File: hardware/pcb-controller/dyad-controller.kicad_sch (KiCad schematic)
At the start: 40 parts, among them J1 USB_C_Receptacle_USB2.0, J10 USB-C split link, J2 SWD, J6 HC-FPC-0.5-20P-FH20, J7 HC-FPC-0.5-20P-FH20, J8 HC-FPC-0.5-14P-FH20, J9 USB-C split link, SW1 SW_Push, U1 W25Q128JVS, U2 USBLC6-2SC6, U3 RP2040, U4 XC6206PxxxMR-Regulator_Linear, Y1 12MHz

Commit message: Fit real BOOTSEL and RESET buttons
CONTROLLER.md §4 items 2 and 3, the two it flags as "would ship a broken or
unflashable board if missed".

SW1's BOOTSEL "switch" was a PinSocket_1x02 header inherited from the dev
board -- a pin header you short with tweezers, not a button. It now carries
Button_Switch_SMD:SW_Push_1P1T_XKB_TS-1187A. SW2 is new, from ~{RESET} to
GND; ~{RESET} is the RP2040's RUN (U3 pin 26), already pulled up by R2 and
brought out to the SWD header, so the button only has to pull it down.

Part: TS-1187A-B-A-B, C318884, JLCPCB **Basic** with 679k stock, 5.1 x 5.1 mm
SMD. One BOM line covers both buttons. KiCad ships a footprint for exactly
this family, and its pads are numbered 1,1,2,2 rather than 1,2,3,4, so the
2-pin SW_Push symbol maps onto the 4-pad part without a symbol change.
Chosen over the TS-1187A-S16 and K2-1114SA alternatives, which are Extended
with 3k-56k stock.

One self-inflicted warning, found and fixed rather than committed: wiring
SW2 raised same_local_global_label, because ~{RESET} exists as a *global*
label on this sheet while batch_connect_to_net only writes local ones.
Replaced with a global label; the warning cleared and the net reads back as
U3 pin 26 + R2 + J2 + SW2. Recorded in §5 step 3 as a trap for the next
signal wired to a global label.

Numbers: errors unchanged at 3, still only GPIO27-29, the genuine spares.
Every other count identical -- endpoint_off_grid 92, lib_symbol_mismatch 48.
0 shorts, 0 orphans.

That closes every unconditional item in §4 except the DNP level shifter. The
only other outstanding change is the LDO swap, which is gated on a Phase 1
current measurement.

Co-Authored-By: Claude Opus 5 <noreply@anthropic.com>
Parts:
- added SW2: RESET, Button_Switch_SMD:SW_Push_1P1T_XKB_TS-1187A, symbol Switch:SW_Push
- SW1: value SW_Push -> BOOTSEL; footprint Connector_PinSocket_2.54mm:PinSocket_1x02_P2.54mm_Vertical -> Button_Switch_SMD:SW_Push_1P1T_XKB_TS-1187A; LCSC (none) -> C318884
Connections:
- net GND: now also SW2.2
- net ~{RESET}: now also SW2.1
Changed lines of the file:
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@@
 		)
 	)
+	(label "VBUS_FUSED"
+		(at 272.415 29.21 0)
+		(effects
+			(font
+				(size 1.27 1.27)
+			)
+			(justify left bottom)
+		)
+	)
+	(label "VBUS_FUSED"
+		(at 144.78 175.26 0)
+		(effects
+			(font
+				(size 1.27 1.27)
+			)
+			(justify left bottom)
+		)
+	)
+	(label "+5V"
+		(at 137.16 175.26 180)
+		(effects
+			(font
+				(size 1.27 1.27)
+			)
+			(justify right bottom)
+		)
+	)
+	(label "+5V"
+		(at 140.97 199.39 0)
+		(effects
+			(font
+				(size 1.27 1.27)
+			)
+			(justify left bottom)
+		)
+	)
+	(label "VBUS_SPLIT"
+		(at 140.97 194.31 0)
+		(effects
+			(font
+				(size 1.27 1.27)
+			)
+			(justify left bottom)
+		)
+	)
+	(label "GND"
+		(at 146.05 218.44 0)
+		(effects
+			(font
+				(size 1.27 1.27)
+			)
+			(justify left bottom)
+		)
+	)
 	(global_label "SWCLK"
 		(shape input)
@@
 		)
 	)
-  (label "VBUS_FUSED"
-    (at 272.415 29.21 0)
-    (fields_autoplaced yes)
-    (effects (font (size 1.27 1.27)) (justify left bottom))
-  )
-  (label "VBUS_FUSED"
-    (at 144.78 175.26 0)
-    (fields_autoplaced yes)
-    (effects (font (size 1.27 1.27)) (justify left bottom))
-  )
-  (label "+5V"
-    (at 137.16 175.26 180)
-    (fields_autoplaced yes)
-    (effects (font (size 1.27 1.27)) (justify right bottom))
-  )
-  (label "+5V"
-    (at 140.97 199.39 0)
-    (fields_autoplaced yes)
-    (effects (font (size 1.27 1.27)) (justify left bottom))
-  )
-  (label "VBUS_SPLIT"
-    (at 140.97 194.31 0)
-    (fields_autoplaced yes)
-    (effects (font (size 1.27 1.27)) (justify left bottom))
-  )
+	(global_label "~{RESET}"
+		(shape input)
+		(at 135.89 218.44 180)
+		(effects
+			(font
+				(size 1.27 1.27)
+			)
+			(justify right)
+		)
+	)
 	(symbol
 		(lib_id "Device:R_Small")
@@
 			)
 		)
-		(property "Value" "SW_Push"
+		(property "Value" "BOOTSEL"
 			(at 118.11 21.59 0)
 			(show_name no)
@@
 			)
 		)
-		(property "Footprint" "Connector_PinSocket_2.54mm:PinSocket_1x02_P2.54mm_Vertical"
+		(property "Footprint" "Button_Switch_SMD:SW_Push_1P1T_XKB_TS-1187A"
 			(at 118.11 21.59 0)
 			(hide yes)
@@
 			)
 		)
+		(property "LCSC" "C318884"
+			(at 118.11 26.67 0)
+			(hide yes)
+			(effects
+				(font
+					(size 1.27 1.27)
+				)
+			)
+		)
 		(body_style 1)
 		(in_pos_files yes)
@@
 			)
 		)
-		(instances
-			(project "dyad-controller"
-				(path "/ba62e47e-9e07-4e97-ab08-24b670d50f97"
-					(reference "D1")
-					(unit 1)
-				)
-			)
-		)
 		(property "LCSC" "C8678"
 			(at 140.97 175.26 0)
@@
 				)
 			)
-		))
+		)
+		(instances
+			(project "dyad-controller"
+				(path "/ba62e47e-9e07-4e97-ab08-24b670d50f97"
+					(reference "D1")
+					(unit 1)
+				)
+			)
+		)
+	)
 	(symbol
 		(lib_id "Device:Polyfuse_Small")
@@
 			)
 		)
+		(property "LCSC" "C70076"
+			(at 140.97 196.85 0)
+			(hide yes)
+			(effects
+				(font
+					(size 1.27 1.27)
+				)
+			)
+		)
 		(instances
 			(project "dyad-controller"
@@
 			)
 		)
-		(property "LCSC" "C70076"
-			(at 140.97 196.85 0)
+	)
+	(symbol
+		(lib_id "Switch:SW_Push")
+		(at 140.97 218.44 0)
+		(unit 1)
+		(in_bom yes)
+		(on_board yes)
+		(dnp no)
+		(property "Reference" "SW2"
+			(at 142.24 215.9 0)
+			(effects
+				(font
+					(size 1.27 1.27)
+				)
+				(justify left)
+			)
+		)
+		(property "Value" "RESET"
+			(at 140.97 219.964 0)
+			(effects
+				(font
+					(size 1.27 1.27)
+				)
+			)
+		)
+		(property "Footprint" "Button_Switch_SMD:SW_Push_1P1T_XKB_TS-1187A"
+			(at 140.97 218.44 0)
+			(hide yes)
+			(effects
+				(font
+					(size 1.27 1.27)
+				)
+			)
+		)
+		(property "Datasheet" ""
+			(at 140.97 218.44 0)
+			(hide yes)
+			(effects
+				(font
+					(size 1.27 1.27)
+				)
+			)
+		)
+		(property "Description" "Push button switch, generic, two pins"
+			(at 140.97 218.44 0)
 			(hide yes)
 			(effects
@@
 				)
 			)
-		))
+		)
+		(property "LCSC" "C318884"
+			(at 140.97 218.44 0)
+			(hide yes)
+			(effects
+				(font
+					(size 1.27 1.27)
+				)
+			)
+		)
+		(instances
+			(project "dyad-controller"
+				(path "/ba62e47e-9e07-4e97-ab08-24b670d50f97"
+					(reference "SW2")
+					(unit 1)
+				)
+			)
+		)
+	)
 	(polyline
 		(pts

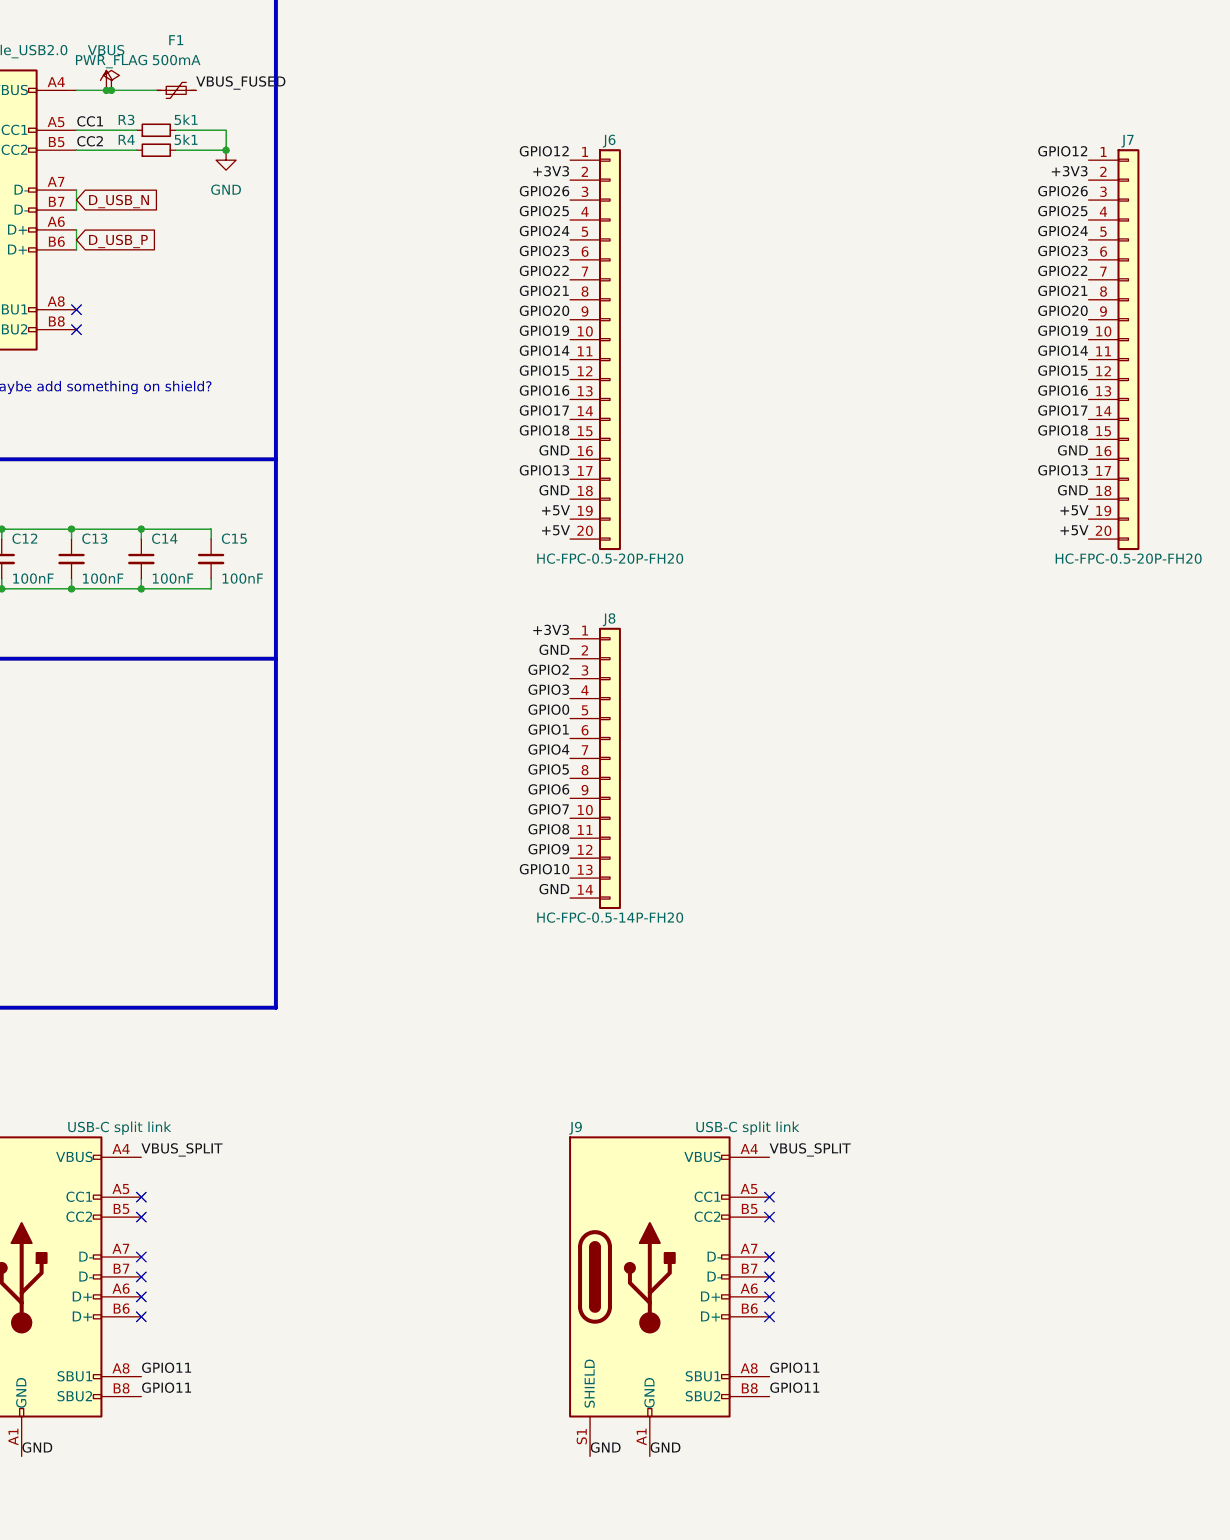
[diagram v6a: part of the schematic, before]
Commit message: Reassign the controller GPIOs to match the board's geometry
The first pin map predated any placement and put the knob bus on the side
of the RP2040 facing away from the knob FFC. With parts on B.Cu, a 35 x 50
board and U3's USB face toward the rear, the knob now takes GP16-26 off the
front-left corner, keeping the SPI0/I2C0 dual-function pair on GP16/GP17,
and the matrix, LEDIN and SPLIT take GP0-15 as one bundle already in J7's
pad order. GP27-29 stay spare and ADC-capable.

Applied by renaming only the connector-side net labels, so U3's labels
still name the physical pin. J8 pins 3-6 reorder to D0, D1, SCK, MOSI; the
knob module does not exist yet. Netlist verified pin by pin; ERC unchanged
at 152 findings with the same 3 errors.

CONTROLLER.md records the map, the connector pin-1 geometry it was derived
from, and the routing consequence: J6 is reached by wrapping the bundle
around the rear of the chip, which supplies the order reversal J6 needs,
at the cost of about one layer change per net.

Co-Authored-By: Claude Opus 5.5 <noreply@anthropic.com>
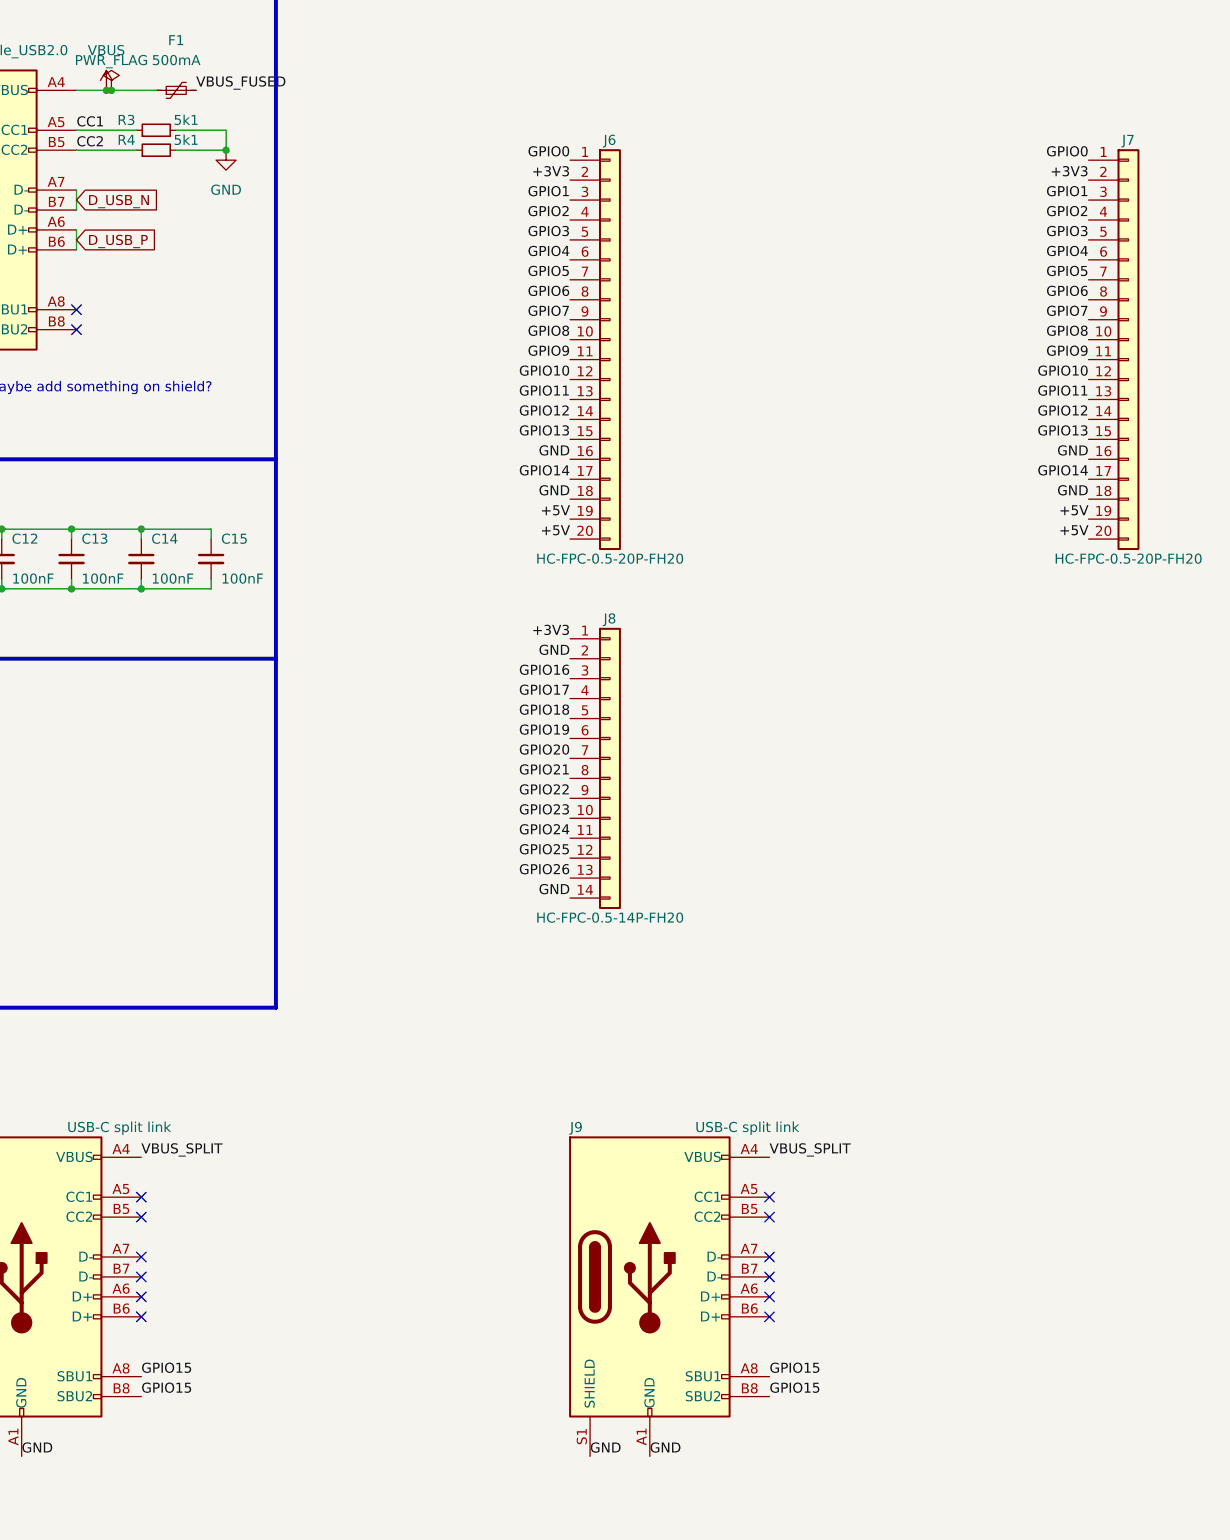
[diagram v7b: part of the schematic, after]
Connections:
- net GPIO0: now also J6.1 (Pin_1), J7.1 (Pin_1); no longer J8.5 (Pin_5)
- net GPIO1: now also J6.3 (Pin_3), J7.3 (Pin_3); no longer J8.6 (Pin_6)
- net GPIO10: now also J6.12 (Pin_12), J7.12 (Pin_12); no longer J8.13 (Pin_13)
- net GPIO11: now also J6.13 (Pin_13), J7.13 (Pin_13); no longer J10.A8 (SBU1), J10.B8 (SBU2), J9.A8 (SBU1), J9.B8 (SBU2)
- net GPIO12: now also J6.14 (Pin_14), J7.14 (Pin_14); no longer J6.1 (Pin_1), J7.1 (Pin_1)
- net GPIO13: now also J6.15 (Pin_15), J7.15 (Pin_15); no longer J6.17 (Pin_17), J7.17 (Pin_17)
- net GPIO14: now also J6.17 (Pin_17), J7.17 (Pin_17); no longer J6.11 (Pin_11), J7.11 (Pin_11)
- net GPIO15: now also J10.A8 (SBU1), J10.B8 (SBU2), J9.A8 (SBU1), J9.B8 (SBU2); no longer J6.12 (Pin_12), J7.12 (Pin_12)
- net GPIO16: now also J8.3 (Pin_3); no longer J6.13 (Pin_13), J7.13 (Pin_13)
- net GPIO17: now also J8.4 (Pin_4); no longer J6.14 (Pin_14), J7.14 (Pin_14)
- net GPIO18: now also J8.5 (Pin_5); no longer J6.15 (Pin_15), J7.15 (Pin_15)
- net GPIO19: now also J8.6 (Pin_6); no longer J6.10 (Pin_10), J7.10 (Pin_10)
- net GPIO2: now also J6.4 (Pin_4), J7.4 (Pin_4); no longer J8.3 (Pin_3)
- net GPIO20: now also J8.7 (Pin_7); no longer J6.9 (Pin_9), J7.9 (Pin_9)
- net GPIO21: now also J8.8 (Pin_8); no longer J6.8 (Pin_8), J7.8 (Pin_8)
- net GPIO22: now also J8.9 (Pin_9); no longer J6.7 (Pin_7), J7.7 (Pin_7)
- net GPIO23: now also J8.10 (Pin_10); no longer J6.6 (Pin_6), J7.6 (Pin_6)
- net GPIO24: now also J8.11 (Pin_11); no longer J6.5 (Pin_5), J7.5 (Pin_5)
- net GPIO25: now also J8.12 (Pin_12); no longer J6.4 (Pin_4), J7.4 (Pin_4)
- net GPIO26: now also J8.13 (Pin_13); no longer J6.3 (Pin_3), J7.3 (Pin_3)
- net GPIO3: now also J6.5 (Pin_5), J7.5 (Pin_5); no longer J8.4 (Pin_4)
- net GPIO4: now also J6.6 (Pin_6), J7.6 (Pin_6); no longer J8.7 (Pin_7)
- net GPIO5: now also J6.7 (Pin_7), J7.7 (Pin_7); no longer J8.8 (Pin_8)
- net GPIO6: now also J6.8 (Pin_8), J7.8 (Pin_8); no longer J8.9 (Pin_9)
- net GPIO7: now also J6.9 (Pin_9), J7.9 (Pin_9); no longer J8.10 (Pin_10)
- net GPIO8: now also J6.10 (Pin_10), J7.10 (Pin_10); no longer J8.11 (Pin_11)
- net GPIO9: now also J6.11 (Pin_11), J7.11 (Pin_11); no longer J8.12 (Pin_12)

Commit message: Sync the controller PCB with its schematic
The board still carried the upstream reference layout. Cleared its 433
tracks and 32 vias (routed for the 45 x 93 mm board and the old pin map)
and the J3/J4/J5 breakout headers, then added D1, F2, J6-J10 and SW2 from
the schematic, and swapped SW1 from a pin header to the TS-1187A button.

USB-C: the stock USB_C_Receptacle_USB2.0 symbol numbers its shield pin S1,
but KiCad 10's HRO TYPE-C-31-M-12 footprint names those pads SH, so J9/J10
could not be placed with their shield on GND. J1 only worked because it was
the KiCad 6 copy, which still said S1. Added dyad:USB_C_Receptacle_HRO_TYPE-
C-31-M-12 with the shield pads renumbered S1 and pointed J1, J9 and J10 at it.

SW1 fixes: Change Footprint netted only one pad of each duplicate-numbered
pair (the TS-1187A pads are 1,1,2,2), so all four are now netted by hand. It
was also excluded from the BOM -- in the schematic too, inherited from the
header -- which would have left the BOOTSEL button unfitted. Now in_bom yes,
value BOOTSEL.

Verified: 41/41 footprints and 41/41 footprint IDs match the schematic, and
all 246 schematic pins land on correctly netted pads. ERC unchanged at 152.
Parity leaves 14 field-copy differences (LCSC, Datasheet, Serves). The new
parts sit stacked off-board awaiting the 35 x 50 outline and placement.

Co-Authored-By: Claude Opus 5.5 <noreply@anthropic.com>
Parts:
- J1, J10, J9: footprint Connector_USB:USB_C_Receptacle_HRO_TYPE-C-31-M-12 -> dyad:USB_C_Receptacle_HRO_TYPE-C-31-M-12
- SW1: now in the parts list
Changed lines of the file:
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@@
 		(unit 1)
 		(exclude_from_sim no)
-		(in_bom no)
+		(in_bom yes)
 		(on_board yes)
 		(dnp no)
@@
 			)
 		)
-		(property "Footprint" "Connector_USB:USB_C_Receptacle_HRO_TYPE-C-31-M-12"
+		(property "Footprint" "dyad:USB_C_Receptacle_HRO_TYPE-C-31-M-12"
 			(at 245.745 44.45 0)
 			(hide yes)
@@
 			)
 		)
-		(property "Footprint" "Connector_USB:USB_C_Receptacle_HRO_TYPE-C-31-M-12"
+		(property "Footprint" "dyad:USB_C_Receptacle_HRO_TYPE-C-31-M-12"
 			(at 330.2 180.34 0)
 			(hide yes)
@@
 			)
 		)
-		(property "Footprint" "Connector_USB:USB_C_Receptacle_HRO_TYPE-C-31-M-12"
+		(property "Footprint" "dyad:USB_C_Receptacle_HRO_TYPE-C-31-M-12"
 			(at 250.19 180.34 0)
 			(hide yes)
